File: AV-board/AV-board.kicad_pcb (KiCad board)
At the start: 2 copper layers, 25 parts, among them J1 Mini-DIN-8, Q1 BC547, Q2 BC547, Q3 BC547, Q4 BC547, U2 74LS241

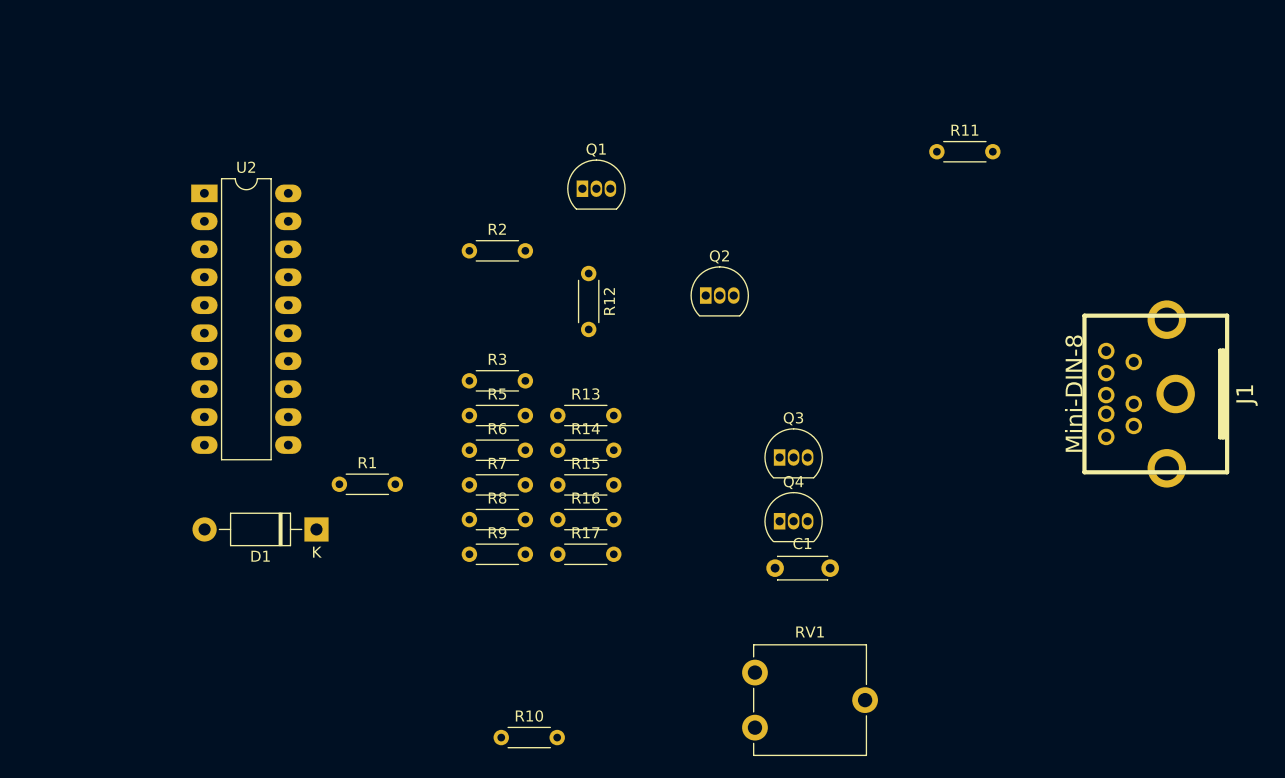
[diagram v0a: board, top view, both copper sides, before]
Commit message: AudioVideo board like Harlequin for any ZX Clone
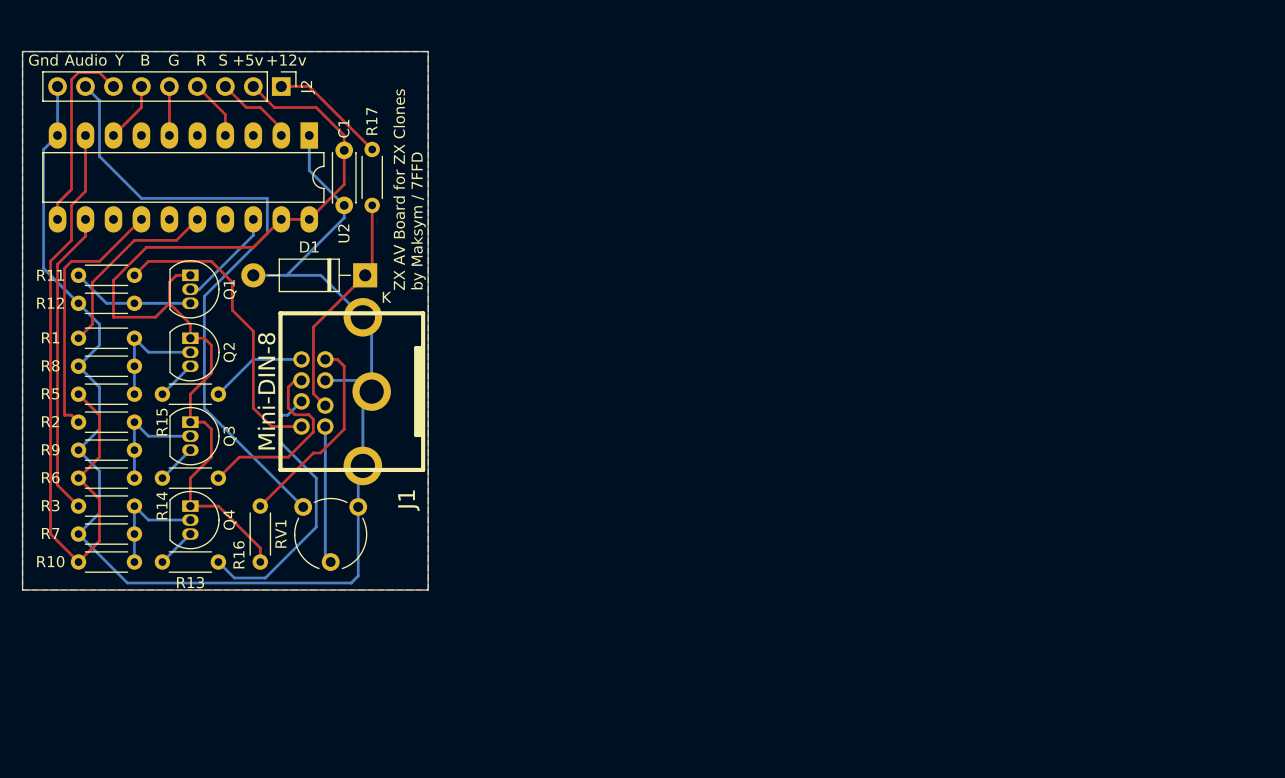
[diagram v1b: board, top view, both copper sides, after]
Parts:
- added J2: Conn_01x09_Pin, Connector_PinHeader_2.54mm:PinHeader_1x09_P2.54mm_Vertical, F.Cu at (70.5, 55.9)
- RV1: footprint Potentiometer_THT:Potentiometer_ACP_CA9-V10_Vertical -> Potentiometer_THT:Potentiometer_Piher_PT-6-V_Vertical
- moved R11 78.8 mm to (52.1, 73.0)
- moved J1 73.0 mm to (76.9, 83.6)
- moved C1 54.5 mm to (76.2, 61.7), turned to -90 degrees
- moved Q3 53.6 mm to (62.2, 86.4), turned to -90 degrees
- moved Q4 53.5 mm to (62.2, 94.0), turned to -90 degrees
- moved Q2 47.0 mm to (62.2, 78.7), turned to -90 degrees
- moved RV1 45.7 mm to (72.5, 94.1), turned to -90 degrees
- moved R12 41.3 mm to (57.1, 75.6), turned to 180 degrees
- moved R17 40.4 mm to (78.7, 61.6), turned to -90 degrees
- moved R2 38.8 mm to (52.1, 86.4)
- moved R13 38.3 mm to (59.7, 99.1)
- moved R10 38.1 mm to (57.1, 96.5), turned to 180 degrees
- moved R3 37.3 mm to (52.1, 94.0)
- moved R15 36.8 mm to (59.7, 83.8)
- moved Q1 36.5 mm to (62.2, 73.0), turned to -90 degrees
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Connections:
- net +5V renamed /+5V
- J1 pad 10: (no net) -> GND
- J1 pad 11: (no net) -> GND
- J1 pad 9: (no net) -> GND
- R17 pad 1: +12V -> /+12V
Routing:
- net GND: track 0.00 -> 132.9 mm
- net /+5V: track 0.00 -> 85.2 mm
- net Net-(U2-O0b): track 0.00 -> 59.5 mm
- net /AUDIO: track 0.00 -> 57.8 mm
- net Net-(U2-O3a): track 0.00 -> 27.9 mm
- net Net-(J1-Pad8): track 0.00 -> 27.5 mm
- net Net-(J1-Pad7): track 0.00 -> 25.2 mm
- net Net-(U2-O2a): track 0.00 -> 23.7 mm
- net Net-(D1-K): track 0.00 -> 20.8 mm
- net Net-(J1-Pad3): track 0.00 -> 18.2 mm
- net /Y: track 0.00 -> 17.8 mm
- net Net-(J1-Pad4): track 0.00 -> 17.6 mm
- net Net-(U2-O1a): track 0.00 -> 17.5 mm
- net Net-(J1-Pad5): track 0.00 -> 12.5 mm
- net Net-(Q1-E): track 0.00 -> 11.2 mm
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- added copper zone on B.Cu, net GND
- added copper zone on F.Cu, net GND
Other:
- board outline added: 36.8 x 48.9 mm
- board text added: "+12v"
- board text added: "+5v"
- board text added: "Audio"
- board text added: "B"
- board text added: "G"
- board text added: "Gnd"
- board text added: "R"
- board text added: "S"
- board text added: "Y"
- board text added: "ZX AV Board for ZX Clones by Maksym / 7FFD"

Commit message: fixed av-board issues
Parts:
- J1: footprint w_conn_av:minidin-8 -> w_conn_av:minidin-8_1
- Q1, Q2, Q3, Q4: footprint Package_TO_SOT_THT:TO-92_Inline -> Package_TO_SOT_THT:TO-92_Inline_Wide
- moved Q4 2.98 mm to (59.8, 95.7), turned to 0 degrees
- moved Q3 2.95 mm to (59.8, 88.1), turned to 0 degrees
- moved Q2 2.92 mm to (59.8, 80.4), turned to 0 degrees
- moved Q1 2.92 mm to (59.8, 74.6), turned to 0 degrees
- moved J1 0.51 mm to (77.2, 84.0), turned to -90 degrees
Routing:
- net Net-(Q1-E): track 11.2 -> 15.9 mm
- net /+5V: track 85.2 -> 81.9 mm
- net Net-(Q2-E): track 3.59 -> 6.63 mm
- net Net-(Q3-E): track 3.59 -> 6.61 mm
- net Net-(Q4-E): track 3.59 -> 6.57 mm
- net Net-(J1-Pad4): track 17.6 -> 16.0 mm
- net Net-(J1-Pad3): track 18.2 -> 19.1 mm
- net Net-(D1-K): track 20.8 -> 21.3 mm

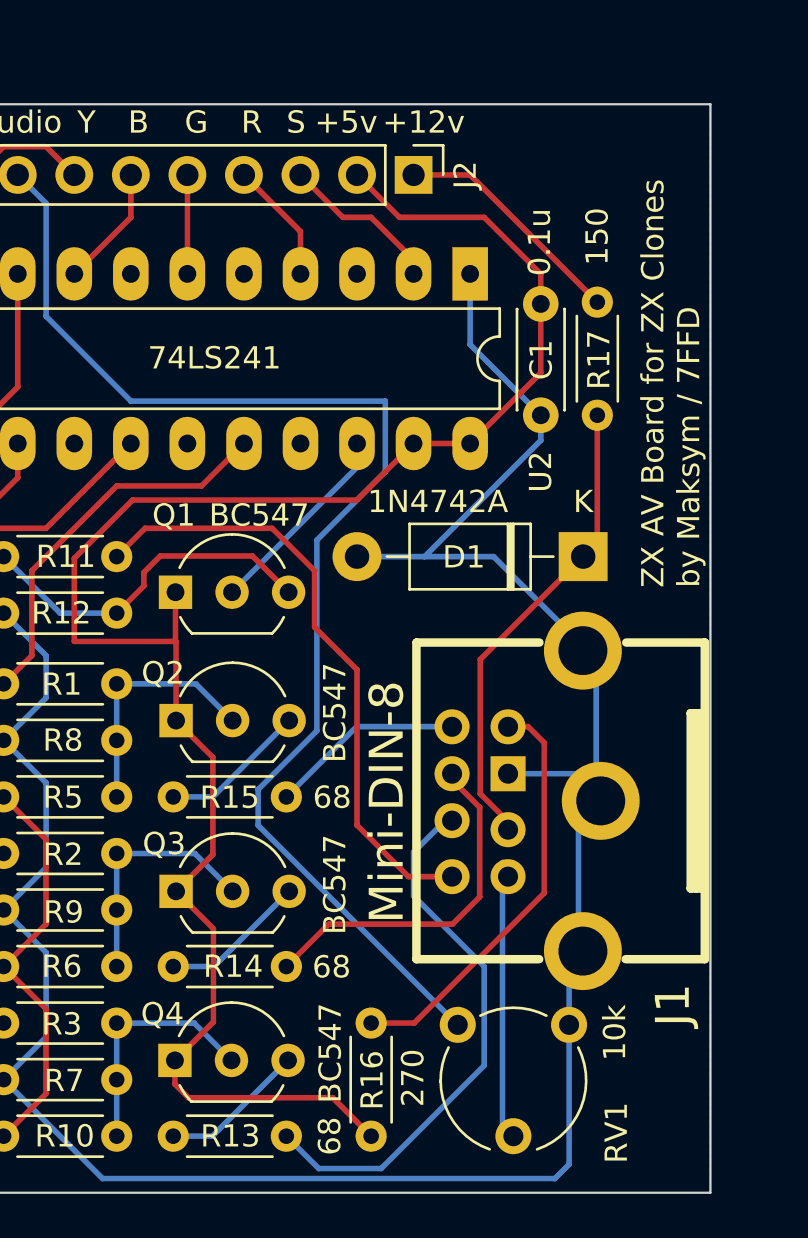
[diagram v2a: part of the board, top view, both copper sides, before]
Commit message: Added capacitor to smooth interference
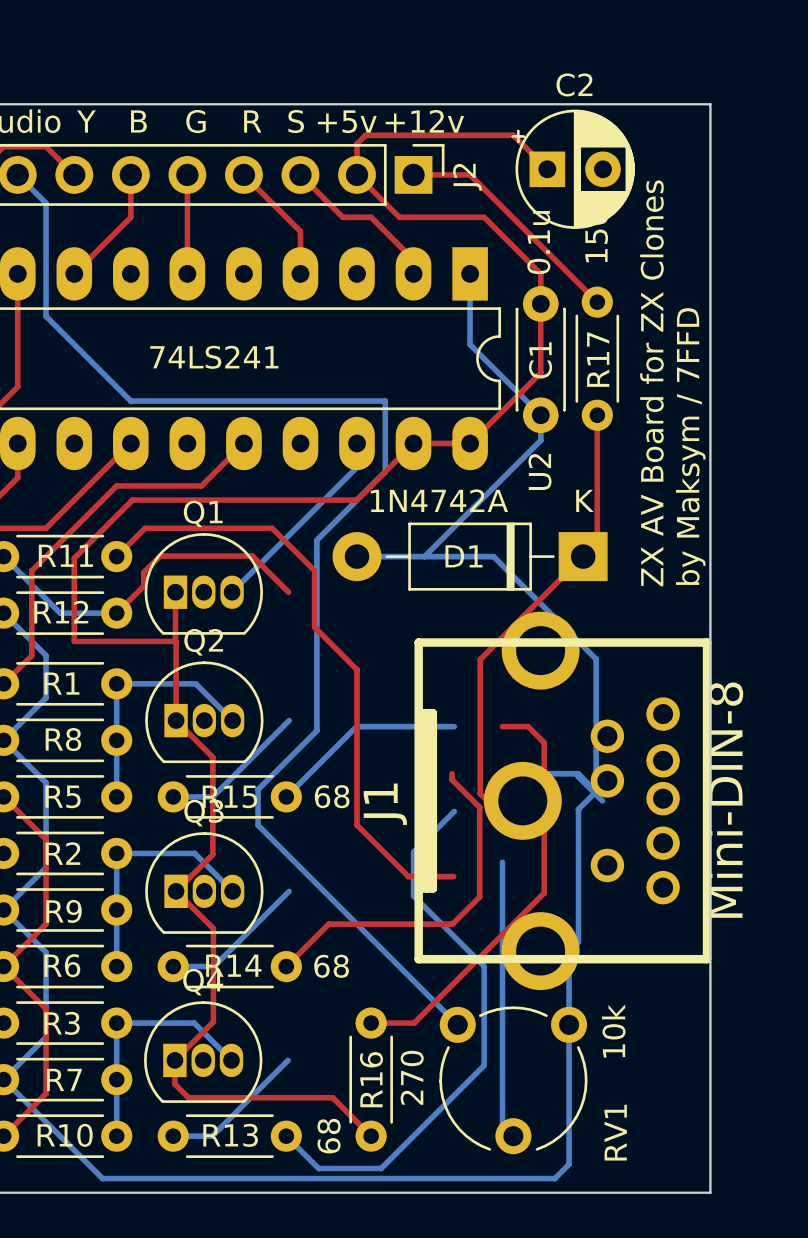
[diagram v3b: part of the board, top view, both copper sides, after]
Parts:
- added C2: 680uF x 16v, Capacitor_THT:CP_Radial_D5.0mm_P2.50mm, F.Cu at (76.5, 55.6)
- J1: footprint w_conn_av:minidin-8_1 -> w_conn_av:minidin-8
- Q1, Q2, Q3, Q4: footprint Package_TO_SOT_THT:TO-92_Inline_Wide -> Package_TO_SOT_THT:TO-92_Inline
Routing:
- net /+5V: track 81.9 -> 92.6 mm
